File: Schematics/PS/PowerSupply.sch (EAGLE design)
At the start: 82 parts, among them IC1 LM317MABDT, IC2 LM337, T1 IRFP240, T2 IRFP240

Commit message: added amages
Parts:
- R7: value 33 -> 330
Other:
- note added: "carlos 1k"
- note added: "carlos 24V"
- note added: "carlos 28V"
- note added: "this is not necessary"
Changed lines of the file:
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@@
 <?xml version="1.0" encoding="utf-8"?>
 <!DOCTYPE eagle SYSTEM "eagle.dtd">
-<eagle version="7.5.0">
+<eagle version="6.5.0">
 <drawing>
 <settings>
@@
 <part name="R5" library="rcl" deviceset="R-US_" device="0617/5V" value="23.5k"/>
 <part name="C2" library="rcl" deviceset="C-EU" device="050-035X075"/>
-<part name="R7" library="rcl" deviceset="R-US_" device="0309/V" value="33"/>
+<part name="R7" library="rcl" deviceset="R-US_" device="0309/V" value="330"/>
 <part name="SGND" library="supply2" deviceset="GND5" device="" value="SGND"/>
 <part name="R12" library="resistor" deviceset="R-US_" device="0207/15" value="100"/>
@@
 <text x="114.3" y="-27.94" size="1.778" layer="97">DNP</text>
 <text x="114.3" y="-40.64" size="1.778" layer="97">DNP</text>
+<text x="152.4" y="-73.66" size="1.778" layer="97">carlos
+1k</text>
+<text x="152.4" y="-58.42" size="1.778" layer="97">carlos
+1k</text>
+<text x="-33.02" y="-25.4" size="1.778" layer="97">this is
+not necessary</text>
+<text x="-22.86" y="-7.62" size="1.778" layer="97">carlos
+28V</text>
+<text x="2.54" y="2.54" size="1.778" layer="97">carlos
+24V</text>
 </plain>
 <instances>

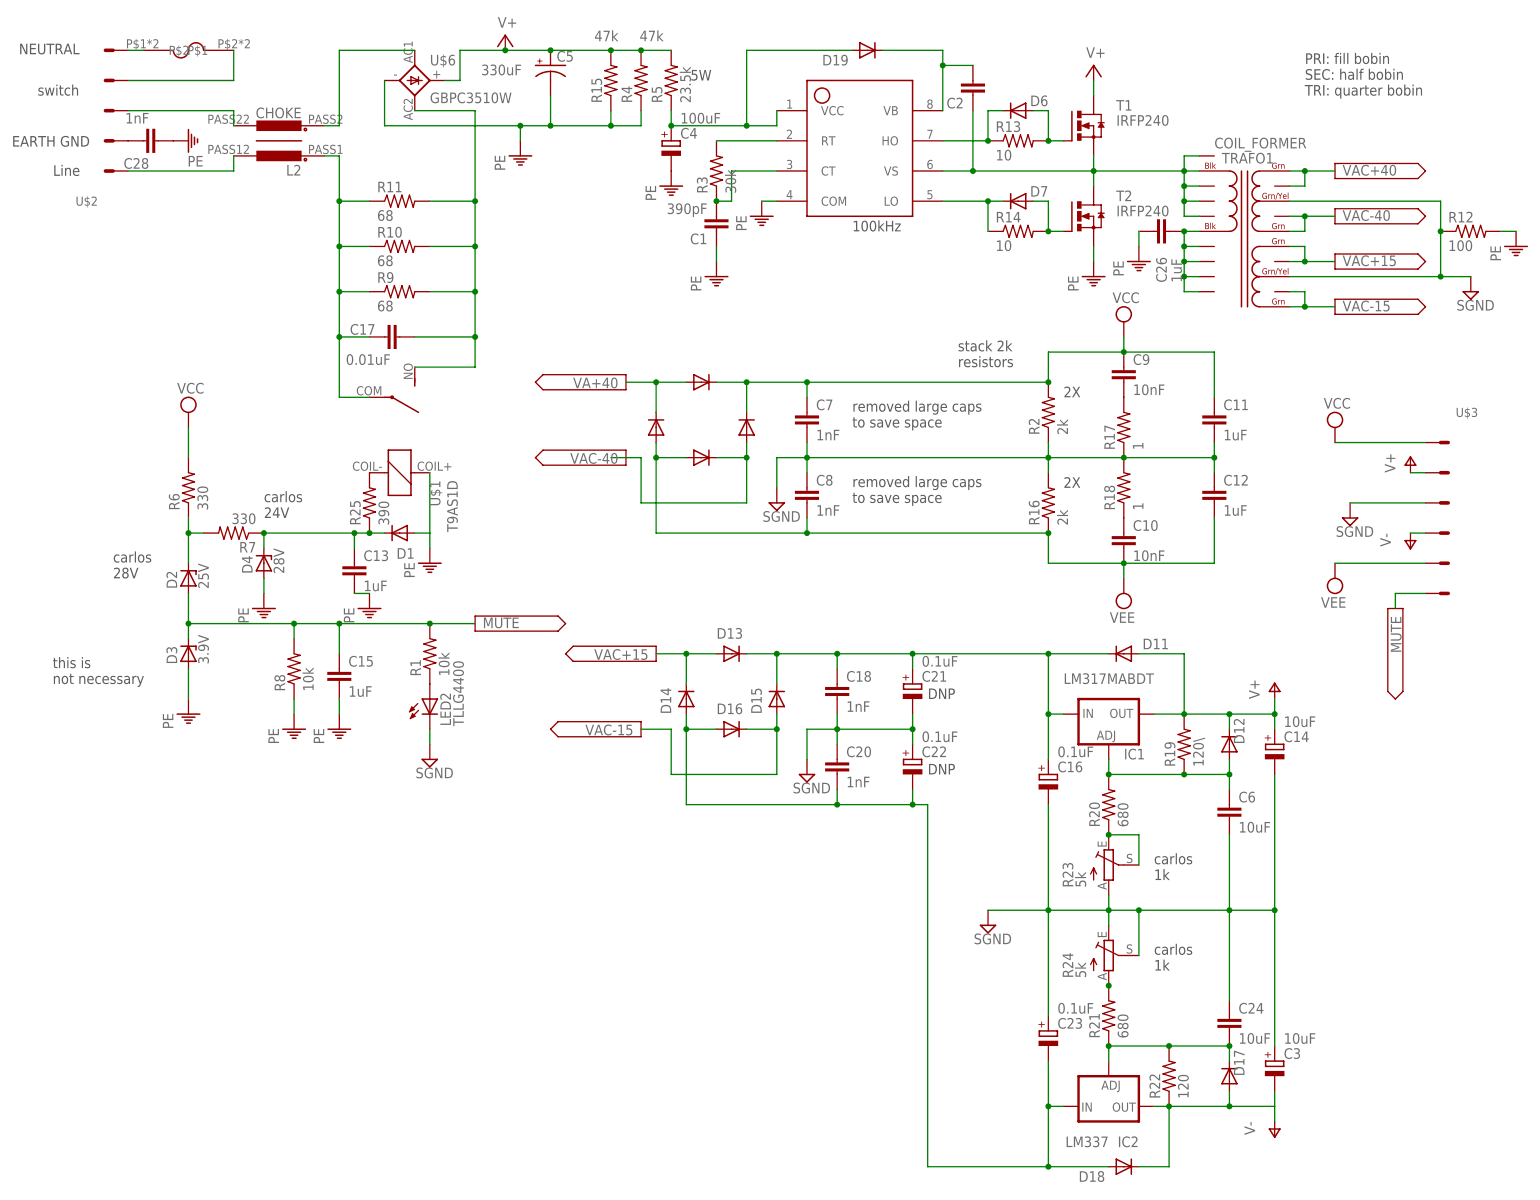
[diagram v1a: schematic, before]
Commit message: removed useless designators on PS schem
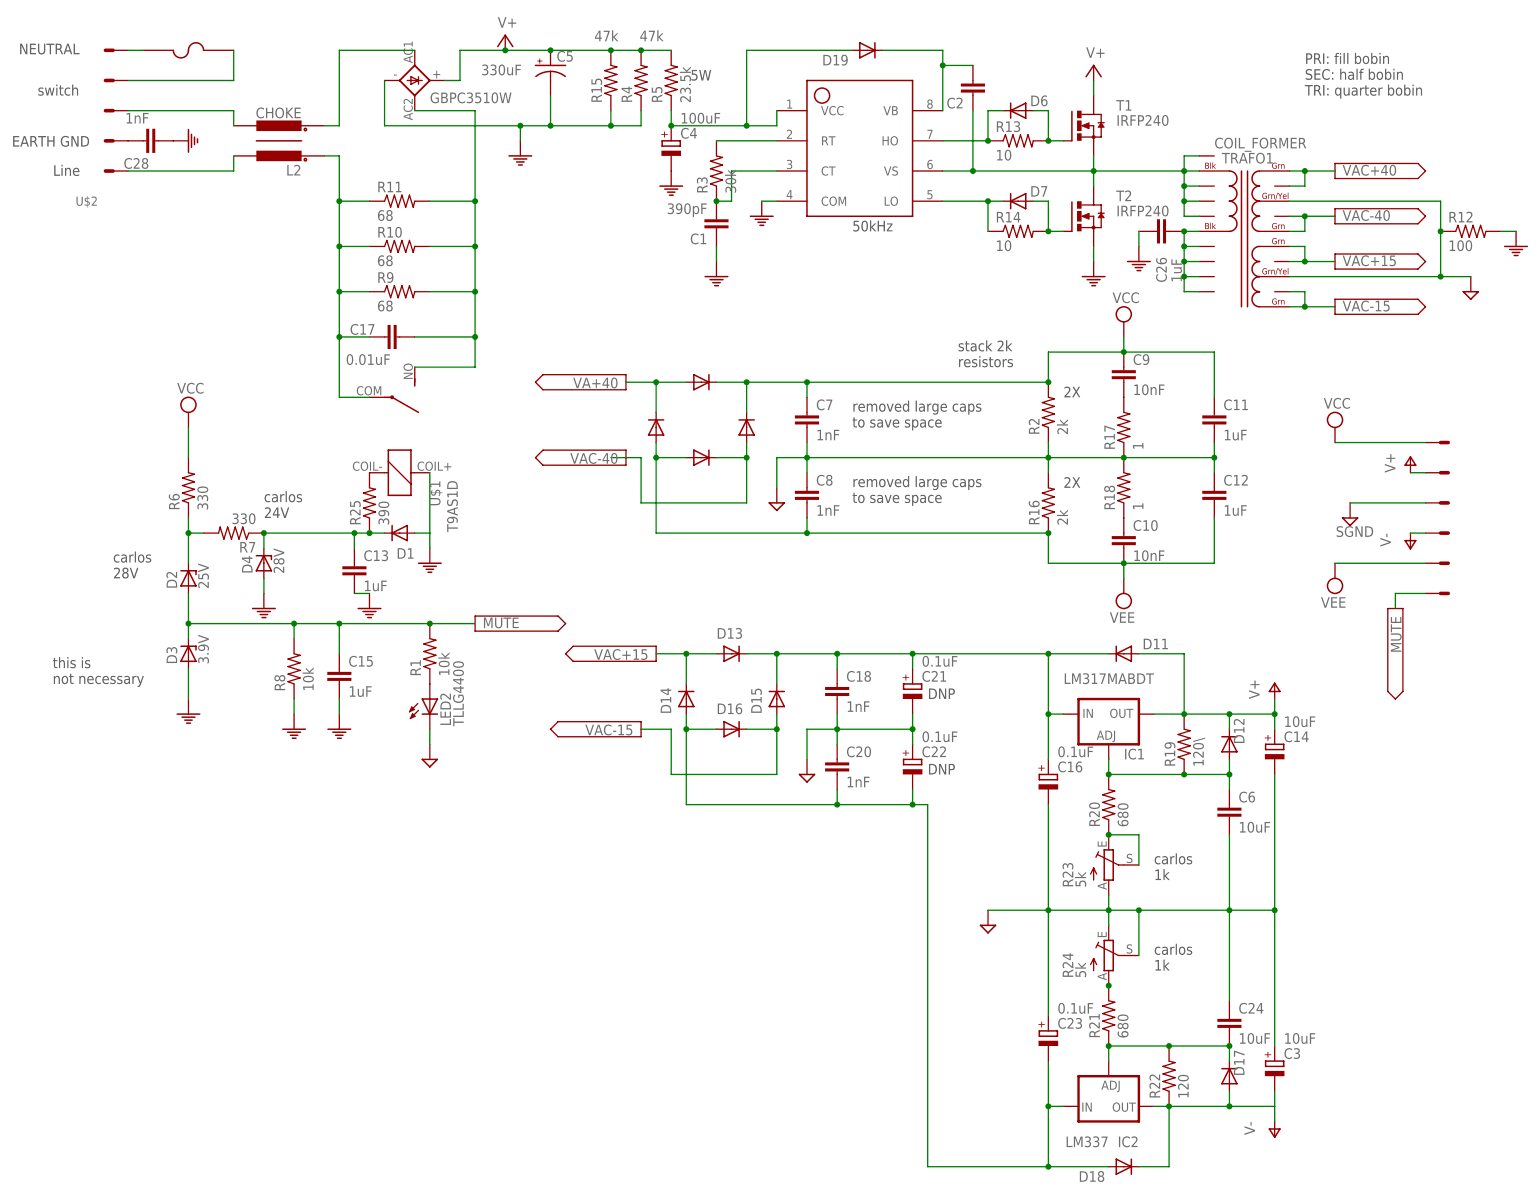
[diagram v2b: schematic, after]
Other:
- note added: "50kHz"
- note removed: "100kHz"
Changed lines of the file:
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@@
 SEC: half bobin
 TRI: quarter bobin</text>
-<text x="101.6" y="50.8" size="1.778" layer="97">100kHz</text>
+<text x="101.6" y="50.8" size="1.778" layer="97">50kHz</text>
 <text x="114.3" y="-27.94" size="1.778" layer="97">DNP</text>
 <text x="114.3" y="-40.64" size="1.778" layer="97">DNP</text>
@@
 <instance part="LED2" gate="G$1" x="30.48" y="-27.94"/>
 <instance part="R1" gate="G$1" x="30.48" y="-20.32" rot="R90"/>
-<instance part="U$4" gate="G$1" x="-10.16" y="81.28"/>
-<instance part="PE1" gate="M" x="-10.16" y="-30.48"/>
-<instance part="PE2" gate="M" x="7.62" y="-33.02"/>
-<instance part="PE3" gate="M" x="15.24" y="-33.02"/>
+<instance part="U$4" gate="G$1" x="-10.16" y="81.28" smashed="yes"/>
+<instance part="PE1" gate="M" x="-10.16" y="-30.48" smashed="yes"/>
+<instance part="PE2" gate="M" x="7.62" y="-33.02" smashed="yes"/>
+<instance part="PE3" gate="M" x="15.24" y="-33.02" smashed="yes"/>
 <instance part="U$2" gate="G$1" x="-22.86" y="68.58" rot="R180"/>
-<instance part="U$3" gate="G$1" x="200.66" y="2.54"/>
-<instance part="PE6" gate="M" x="2.54" y="-12.7"/>
-<instance part="PE8" gate="M" x="30.48" y="-5.08"/>
+<instance part="U$3" gate="G$1" x="200.66" y="2.54" smashed="yes"/>
+<instance part="PE6" gate="M" x="2.54" y="-12.7" smashed="yes"/>
+<instance part="PE8" gate="M" x="30.48" y="-5.08" smashed="yes"/>
 <instance part="U$5" gate="G$1" x="96.52" y="71.12"/>
 <instance part="R3" gate="G$1" x="78.74" y="60.96" rot="R90"/>
 <instance part="C1" gate="G$1" x="78.74" y="50.8" rot="R180"/>
-<instance part="U$6" gate="G$1" x="27.94" y="76.2"/>
-<instance part="PE7" gate="M" x="-10.16" y="66.04" rot="R90"/>
+<instance part="U$6" gate="G$1" x="27.94" y="76.2" smashed="yes">
+<attribute name="VALUE" x="30.48" y="72.39" size="1.778" layer="96"/>
+</instance>
+<instance part="PE7" gate="M" x="-10.16" y="66.04" smashed="yes" rot="R90"/>
 <instance part="C4" gate="G$1" x="71.12" y="66.04" smashed="yes">
 <attribute name="NAME" x="72.644" y="66.421" size="1.778" layer="95"/>
 <attribute name="VALUE" x="72.644" y="68.961" size="1.778" layer="96"/>
 </instance>
-<instance part="PE9" gate="M" x="71.12" y="58.42"/>
-<instance part="PE11" gate="M" x="86.36" y="53.34"/>
-<instance part="PE12" gate="M" x="78.74" y="43.18"/>
+<instance part="PE9" gate="M" x="71.12" y="58.42" smashed="yes"/>
+<instance part="PE11" gate="M" x="86.36" y="53.34" smashed="yes"/>
+<instance part="PE12" gate="M" x="78.74" y="43.18" smashed="yes"/>
 <instance part="T1" gate="G$1" x="142.24" y="68.58"/>
 <instance part="T2" gate="G$1" x="142.24" y="53.34"/>
@@
 <instance part="R14" gate="G$1" x="129.54" y="50.8"/>
 <instance part="TRAFO1" gate="G$1" x="167.64" y="55.88"/>
-<instance part="PE13" gate="M" x="149.86" y="45.72"/>
+<instance part="PE13" gate="M" x="149.86" y="45.72" smashed="yes"/>
 <instance part="SUPPLY4" gate="1" x="142.24" y="78.74"/>
-<instance part="PE14" gate="M" x="142.24" y="43.18"/>
+<instance part="PE14" gate="M" x="142.24" y="43.18" smashed="yes"/>
 <instance part="CP1" gate="1" x="43.18" y="83.82"/>
 <instance part="C5" gate="G$1" x="50.8" y="78.74" smashed="yes">
@@
 <instance part="C2" gate="G$1" x="121.92" y="73.66" rot="R180"/>
 <instance part="R7" gate="G$1" x="-2.54" y="0" rot="R180"/>
-<instance part="SGND" gate="G$1" x="205.74" y="40.64"/>
+<instance part="SGND" gate="G$1" x="205.74" y="40.64" smashed="yes"/>
 <instance part="R12" gate="G$1" x="205.74" y="50.8"/>
 <instance part="SUPPLY5" gate="G$1" x="182.88" y="60.96"/>
@@
 <instance part="D8" gate="G$1" x="68.58" y="17.78" rot="R90"/>
 <instance part="D9" gate="G$1" x="83.82" y="17.78" rot="R90"/>
-<instance part="PE5" gate="M" x="213.36" y="48.26"/>
-<instance part="SGND1" gate="G$1" x="88.9" y="5.08"/>
+<instance part="PE5" gate="M" x="213.36" y="48.26" smashed="yes"/>
+<instance part="SGND1" gate="G$1" x="88.9" y="5.08" smashed="yes"/>
 <instance part="IC1" gate="G$1" x="144.78" y="-30.48" smashed="yes">
 <attribute name="NAME" x="147.32" y="-38.1" size="1.778" layer="95"/>
@@
 <instance part="R20" gate="G$1" x="144.78" y="-45.72" rot="R90"/>
 <instance part="C6" gate="G$1" x="165.1" y="-45.72"/>
-<instance part="SGND2" gate="G$1" x="124.46" y="-66.04"/>
+<instance part="SGND2" gate="G$1" x="124.46" y="-66.04" smashed="yes"/>
 <instance part="C18" gate="G$1" x="99.06" y="-25.4"/>
 <instance part="C20" gate="G$1" x="99.06" y="-38.1"/>
@@
 <instance part="D14" gate="G$1" x="73.66" y="-27.94" rot="R90"/>
 <instance part="D15" gate="G$1" x="88.9" y="-27.94" rot="R90"/>
-<instance part="SGND3" gate="G$1" x="93.98" y="-40.64"/>
+<instance part="SGND3" gate="G$1" x="93.98" y="-40.64" smashed="yes"/>
 <instance part="SUPPLY2" gate="G$1" x="66.04" y="-33.02" rot="R180"/>
 <instance part="C21" gate="G$1" x="111.76" y="-25.4" smashed="yes">
@@
 <instance part="V15+" gate="1" x="195.58" y="12.7"/>
 <instance part="P+2" gate="1" x="172.72" y="-25.4"/>
-<instance part="P-2" gate="1" x="195.58" y="-2.54"/>
+<instance part="P-2" gate="1" x="195.58" y="-2.54" smashed="yes">
+<attribute name="VALUE" x="190.5" y="0" size="1.778" layer="96" rot="R270"/>
+</instance>
 <instance part="SUPPLY14" gate="G$1" x="182.88" y="-7.62" rot="R180"/>
 <instance part="SGND4" gate="G$1" x="185.42" y="2.54"/>
@@
 <attribute name="NAME" x="96.52" y="78.74" size="1.778" layer="95"/>
 </instance>
-<instance part="PE10" gate="M" x="45.72" y="63.5"/>
-<instance part="L2" gate="G$1" x="5.08" y="66.04" rot="R180"/>
+<instance part="PE10" gate="M" x="45.72" y="63.5" smashed="yes"/>
+<instance part="L2" gate="G$1" x="5.08" y="66.04" smashed="yes" rot="R180">
+<attribute name="NAME" x="8.89" y="61.976" size="1.778" layer="95" rot="R180"/>
+<attribute name="VALUE" x="8.89" y="71.628" size="1.778" layer="96" rot="R180"/>
+</instance>
 <instance part="D10" gate="G$1" x="76.2" y="12.7"/>
 <instance part="P-1" gate="1" x="172.72" y="-101.6"/>
@@
 </instance>
 <instance part="C13" gate="G$1" x="17.78" y="-5.08"/>
-<instance part="PE4" gate="M" x="20.32" y="-12.7"/>
+<instance part="PE4" gate="M" x="20.32" y="-12.7" smashed="yes"/>
 <instance part="R23" gate="1" x="144.78" y="-55.88"/>
 <instance part="R24" gate="1" x="144.78" y="-71.12"/>
 <instance part="R25" gate="G$1" x="20.32" y="5.08" rot="R90"/>
-<instance part="SGND5" gate="G$1" x="30.48" y="-38.1"/>
+<instance part="SGND5" gate="G$1" x="30.48" y="-38.1" smashed="yes"/>
 </instances>
 <busses>
